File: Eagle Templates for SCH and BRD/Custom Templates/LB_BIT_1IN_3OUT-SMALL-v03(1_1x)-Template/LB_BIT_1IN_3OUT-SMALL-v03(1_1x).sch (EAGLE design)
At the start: 15 parts, among them U1 LV321SOT23-5

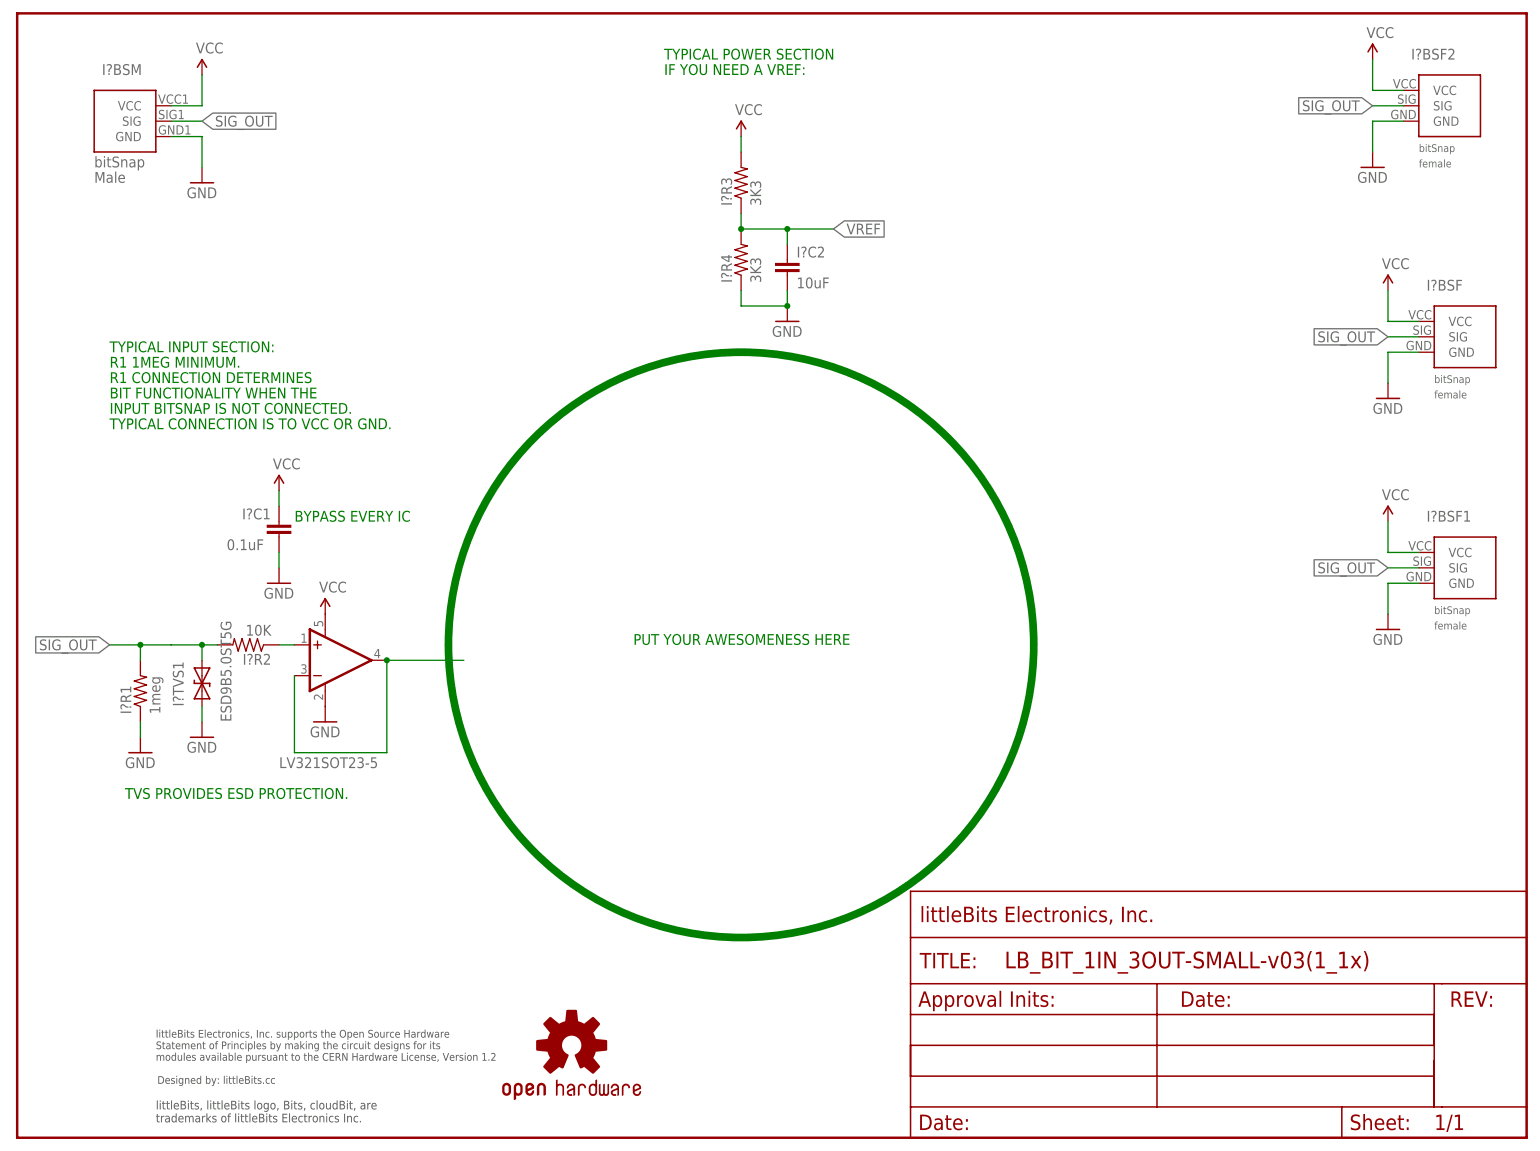
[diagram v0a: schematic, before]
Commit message: Updated templates
- Added ferrite beads
- Moved text and annotations off of Nets layer
- Minor layout changes
- Removed I/O/W prefix from reference designators
- Removed output stage components from output bits
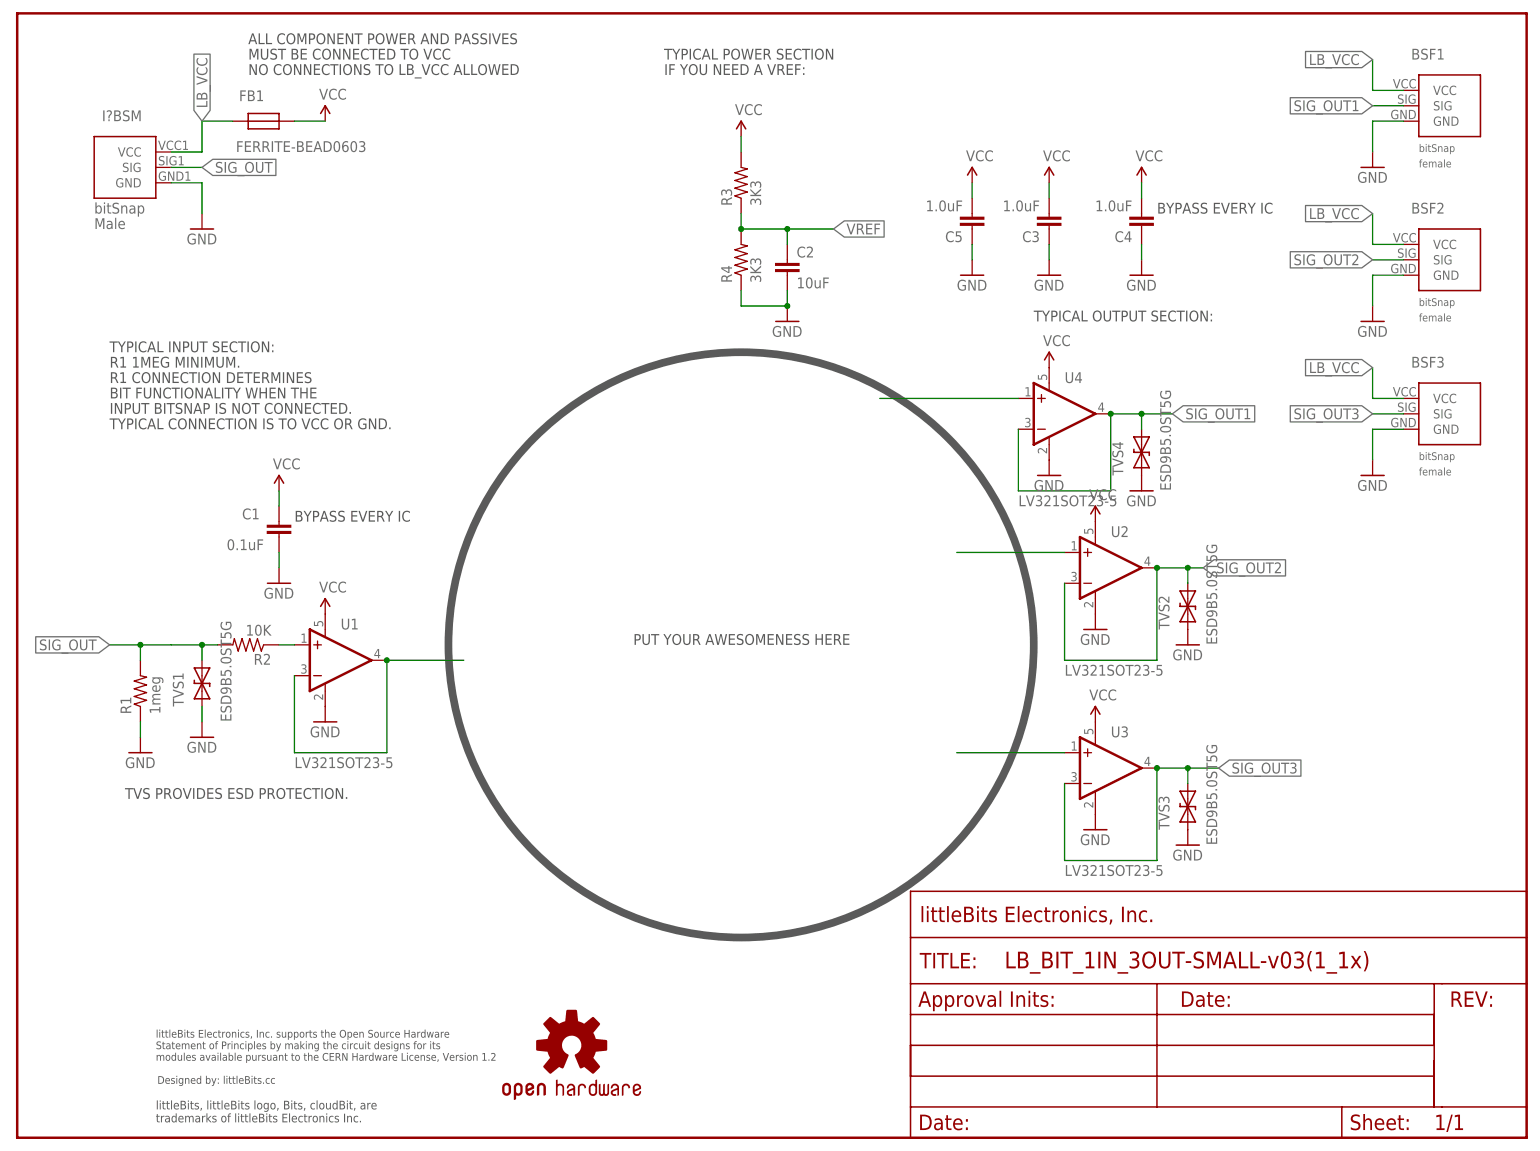
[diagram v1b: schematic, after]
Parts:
- removed I?BSF, I?BSF1: BITSNAP_V03_FEMALE, bitSnap:BITSNAP_V03_FEMALE
- added BSF2, BSF3: BITSNAP_V03_FEMALE, bitSnap:BITSNAP_V03_FEMALE
- added C3, C4, C5: 1.0uF, LITTLEBITS:CAPCAP-0603
- added FB1: FERRITE-BEAD0603, LITTLEBITS:FERRITE-BEAD0603
- added TVS2, TVS3, TVS4: ESD9B5.0ST5G, LITTLEBITS:DIODE-TVSSOD-923
- added U2, U3, U4: LV321SOT23-5, LITTLEBITS:LV321SOT23-5
- renumbered I?BSF2 to BSF1, I?C1 to C1, I?C2 to C2, I?R1 to R1, I?R2 to R2, I?R3 to R3, I?R4 to R4, I?TVS1 to TVS1
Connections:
- new net LB_VCC: BSF1.VCC, BSF2.VCC, BSF3.VCC, FB1.P$2, I?BSM.VCC
- new net N$12: U4.+IN
- new net N$2: U2.+IN
- new net N$5: U3.+IN
- new net SIG_OUT1: BSF1.SIG, TVS4.C, U4.-IN, U4.OUT
- new net SIG_OUT2: BSF2.SIG, TVS2.C, U2.-IN, U2.OUT
- new net SIG_OUT3: BSF3.SIG, TVS3.C, U3.-IN, U3.OUT
- net GND: now also BSF2.GND, BSF3.GND, C3.1, C4.1, C5.1, TVS2.A, TVS3.A, TVS4.A, U2.V-, U3.V-, U4.V-; no longer I?BSF.GND, I?BSF1.GND
- net SIG_OUT: no longer BSF1.SIG, I?BSF.SIG, I?BSF1.SIG
- net VCC: now also C3.2, C4.2, C5.2, FB1.P$1, U2.V+, U3.V+, U4.V+; no longer BSF1.VCC, I?BSF.VCC, I?BSF1.VCC, I?BSM.VCC
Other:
- note added: "ALL COMPONENT POWER AND PASSIVES"
- note added: "MUST BE CONNECTED TO VCC"
- note added: "NO CONNECTIONS TO LB_VCC ALLOWED"
- note added: "TYPICAL OUTPUT SECTION:"
- moved on the sheet: I?BSM
